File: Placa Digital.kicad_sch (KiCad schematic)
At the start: 21 parts, among them J1 Entradas / Salidas, Q1 BC548, Q2 BC548, U1 EC11_Module, U2 Alimentación, U3 ST7920_Display, U4 10K

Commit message: Version V1 (Clearence)
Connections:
- no-connect marks 0 -> 10
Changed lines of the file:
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@@
   (junction (at 224.79 121.92) (diameter 0) (color 0 0 0 0)
   )
+  (no_connect (at 224.79 81.28))
+  (no_connect (at 242.57 81.2292))
+  (no_connect (at 234.95 81.28))
+  (no_connect (at 232.41 81.28))
+  (no_connect (at 237.49 81.28))
+  (no_connect (at 240.03 81.28))
+  (no_connect (at 214.63 81.28))
+  (no_connect (at 219.71 81.28))
+  (no_connect (at 227.33 81.28))
+  (no_connect (at 229.87 81.28))
   (wire (pts (xy 224.79 121.92) (xy 245.11 121.92))
     (stroke (width 0) (type default) (color 0 0 0 0))

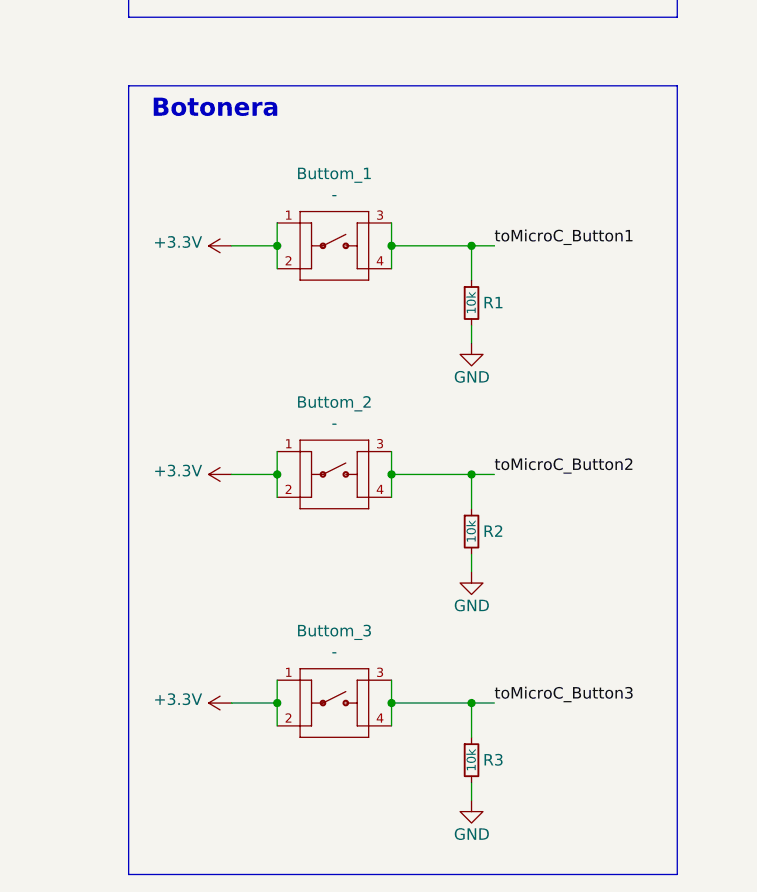
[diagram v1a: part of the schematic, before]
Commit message: Button changed
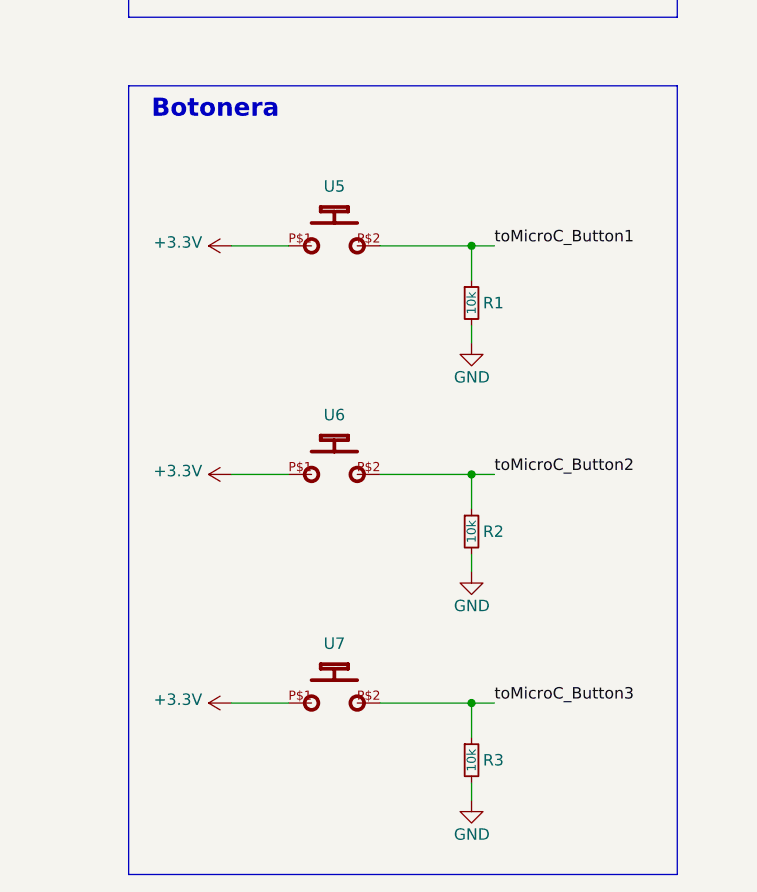
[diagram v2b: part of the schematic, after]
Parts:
- removed Buttom_1, Buttom_2, Buttom_3: -, CEDCp:Pulsador_4Pines, symbol Placa-Digital-rescue:FSM8JH-Pulsador_TH
- added U5, U6, U7: MX1A-11NN, CEDCp:CHERRY_MX1A-11NN_SWITCH, symbol CEDCp:MX1A-11NN
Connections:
- net +3V3: now also U5.P$1, U6.P$1, U7.P$1
- net toMicroC_Button1: now also U5.P$2
- net toMicroC_Button2: now also U6.P$2
- net toMicroC_Button3: now also U7.P$2
